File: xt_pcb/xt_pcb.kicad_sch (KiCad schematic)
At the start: 16 parts, among them J1 Conn_01x04_Socket, U1 AMS1117-3.3, U2 ATmega32U4-A, Y1 Crystal_GND24_Small

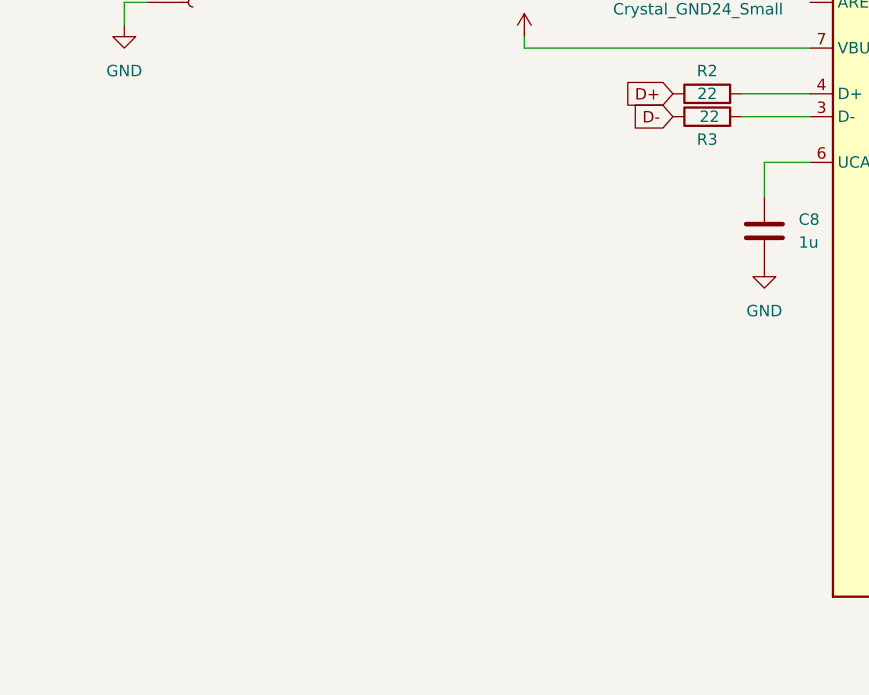
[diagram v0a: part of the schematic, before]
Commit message: Type C Receptible + EDB added
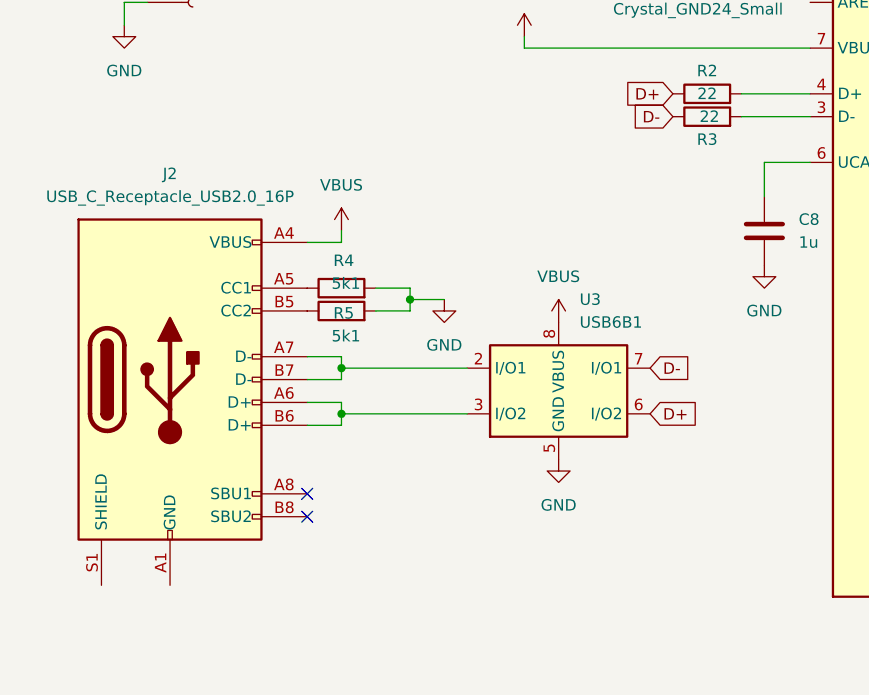
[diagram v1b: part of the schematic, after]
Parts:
- added J2: USB_C_Receptacle_USB2.0_16P, Connector_USB:USB_C_Receptacle_HRO_TYPE-C-31-M-12, symbol Connector:USB_C_Receptacle_USB2.0_16P
- added R4, R5: 5k1, Resistor_SMD:R_0402_1005Metric, symbol Device:R
- added U3: USB6B1, Package_SO:SOIC-8_3.9x4.9mm_P1.27mm, symbol Power_Protection:USB6B1
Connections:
- net D+: now also U3.6 (I/O2)
- net D-: now also U3.7 (I/O1)
- net GND: now also R4.2, R5.2, U3.4 (GND), U3.5 (GND)
- net VBUS: now also J2.A4 (VBUS), J2.A9 (VBUS), J2.B4 (VBUS), J2.B9 (VBUS), U3.1 (VBUS), U3.8 (VBUS)
- new net: J2.B5 (CC2), R5.1
- new net: J2.A7 (D-), J2.B7 (D-), U3.2 (I/O1)
- new net: J2.A6 (D+), J2.B6 (D+), U3.3 (I/O2)
- new net: J2.A1 (GND), J2.A12 (GND), J2.B1 (GND), J2.B12 (GND)
- new net: J2.A5 (CC1), R4.1
- no-connect marks 0 -> 2

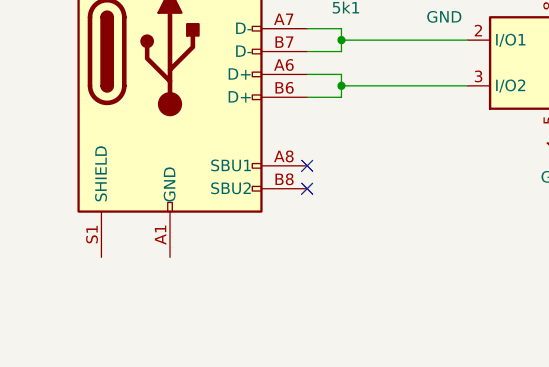
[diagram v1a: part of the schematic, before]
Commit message: basic tracing added to pcb
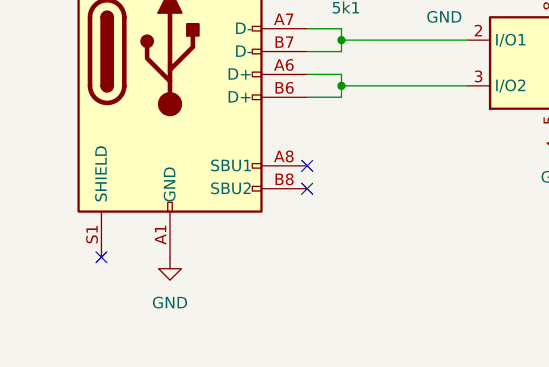
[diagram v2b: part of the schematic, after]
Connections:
- net GND: now also J2.A1 (GND), J2.A12 (GND), J2.B1 (GND), J2.B12 (GND)
- no-connect marks 2 -> 3
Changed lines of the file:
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@@
 	)
 	(no_connect
+		(at 25.4 140.97)
+	)
+	(no_connect
 		(at 48.26 133.35)
 	)
@@
 					(unit 1)
 				)
+			)
+		)
+	)
+	(symbol
+		(lib_id "power:GND")
+		(at 33.02 140.97 0)
+		(unit 1)
+		(exclude_from_sim no)
+		(in_bom yes)
+		(on_board yes)
+		(dnp no)
+		(fields_autoplaced yes)
+		(property "Reference" "#PWR07"
+			(at 33.02 147.32 0)
+			(effects
+				(font
+					(size 1.27 1.27)
+				)
+				(hide yes)
+			)
+		)
+		(property "Value" "GND"
+			(at 33.02 146.05 0)
+			(effects
+				(font
+					(size 1.27 1.27)
+				)
+			)
+		)
+		(property "Footprint" ""
+			(at 33.02 140.97 0)
+			(effects
+				(font
+					(size 1.27 1.27)
+				)
+				(hide yes)
+			)
+		)
+		(property "Datasheet" ""
+			(at 33.02 140.97 0)
+			(effects
+				(font
+					(size 1.27 1.27)
+				)
+				(hide yes)
+			)
+		)
+		(property "Description" "Power symbol creates a global label with name \"GND\" , ground"
+			(at 33.02 140.97 0)
+			(effects
+				(font
+					(size 1.27 1.27)
+				)
+				(hide yes)
+			)
+		)
+		(pin "1"
+		)
+		(instances
+			(project "xt_pcb"
+				(path "/0d76ce34-a40d-405c-820f-030fec8e9950"
+					(reference "#PWR07")
+					(unit 1)
+				)

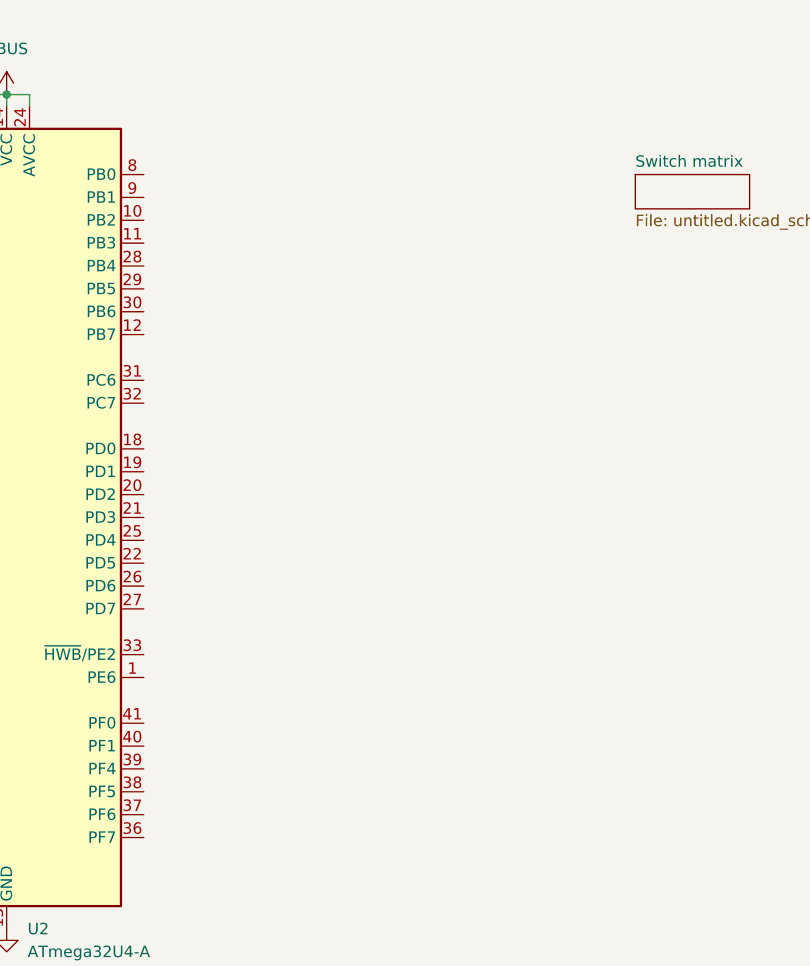
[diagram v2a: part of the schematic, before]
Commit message: Switch matrix labels
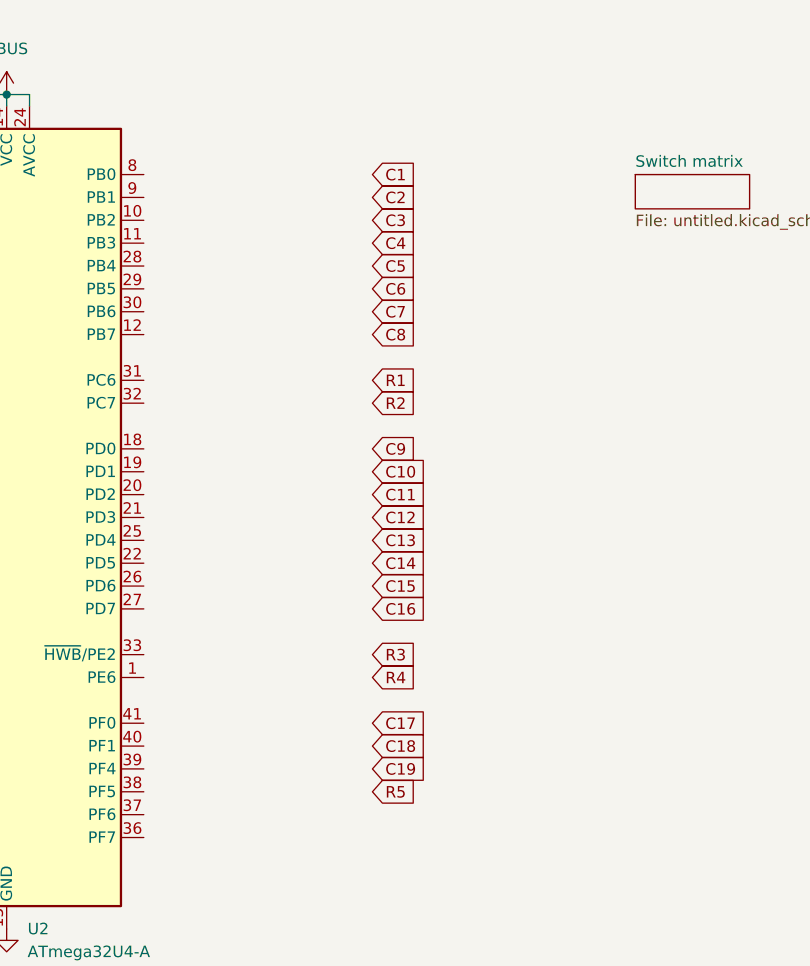
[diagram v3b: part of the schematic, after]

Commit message: tracing finished
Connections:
- net C1: now also U2.11 (PB3)
- net C10: now also U2.29 (PB5)
- net C11: now also U2.30 (PB6)
- net C12: now also U2.31 (PC6)
- net C13: now also U2.32 (PC7)
- net C14: now also U2.33 (~{HWB}/PE2)
- net C15: now also U2.1 (PE6)
- net C16: now also U2.41 (PF0)
- net C17: now also U2.40 (PF1)
- net C18: now also U2.39 (PF4)
- net C19: now also U2.38 (PF5)
- net C2: now also U2.9 (PB1)
- net C3: now also U2.18 (PD0)
- net C4: now also U2.10 (PB2)
- net C5: now also U2.8 (PB0)
- net C6: now also U2.19 (PD1)
- net C7: now also U2.20 (PD2)
- net C8: now also U2.12 (PB7)
- net C9: now also U2.28 (PB4)
- net R1: now also U2.27 (PD7)
- net R2: now also U2.25 (PD4)
- net R3: now also U2.26 (PD6)
- net R4: now also U2.21 (PD3)
- net R5: now also U2.22 (PD5)
